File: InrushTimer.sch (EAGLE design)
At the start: 71 parts, among them IC1 TLC272D, IC2 555, IC3 4076N, Q2 TRANSISTOR-FET_2N7002, Q3 TRANSISTOR-FET_2N7002, Q4 TRANSISTOR-FET_2N7002, Q5 TRANSISTOR-FET_2N7002, Q6 DIODES_ZTX451DIODES_ZTX451_0_0, T1 MMBTA05, U1 ROHM_BY_ELEMENT14_BATCH_1_BU4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

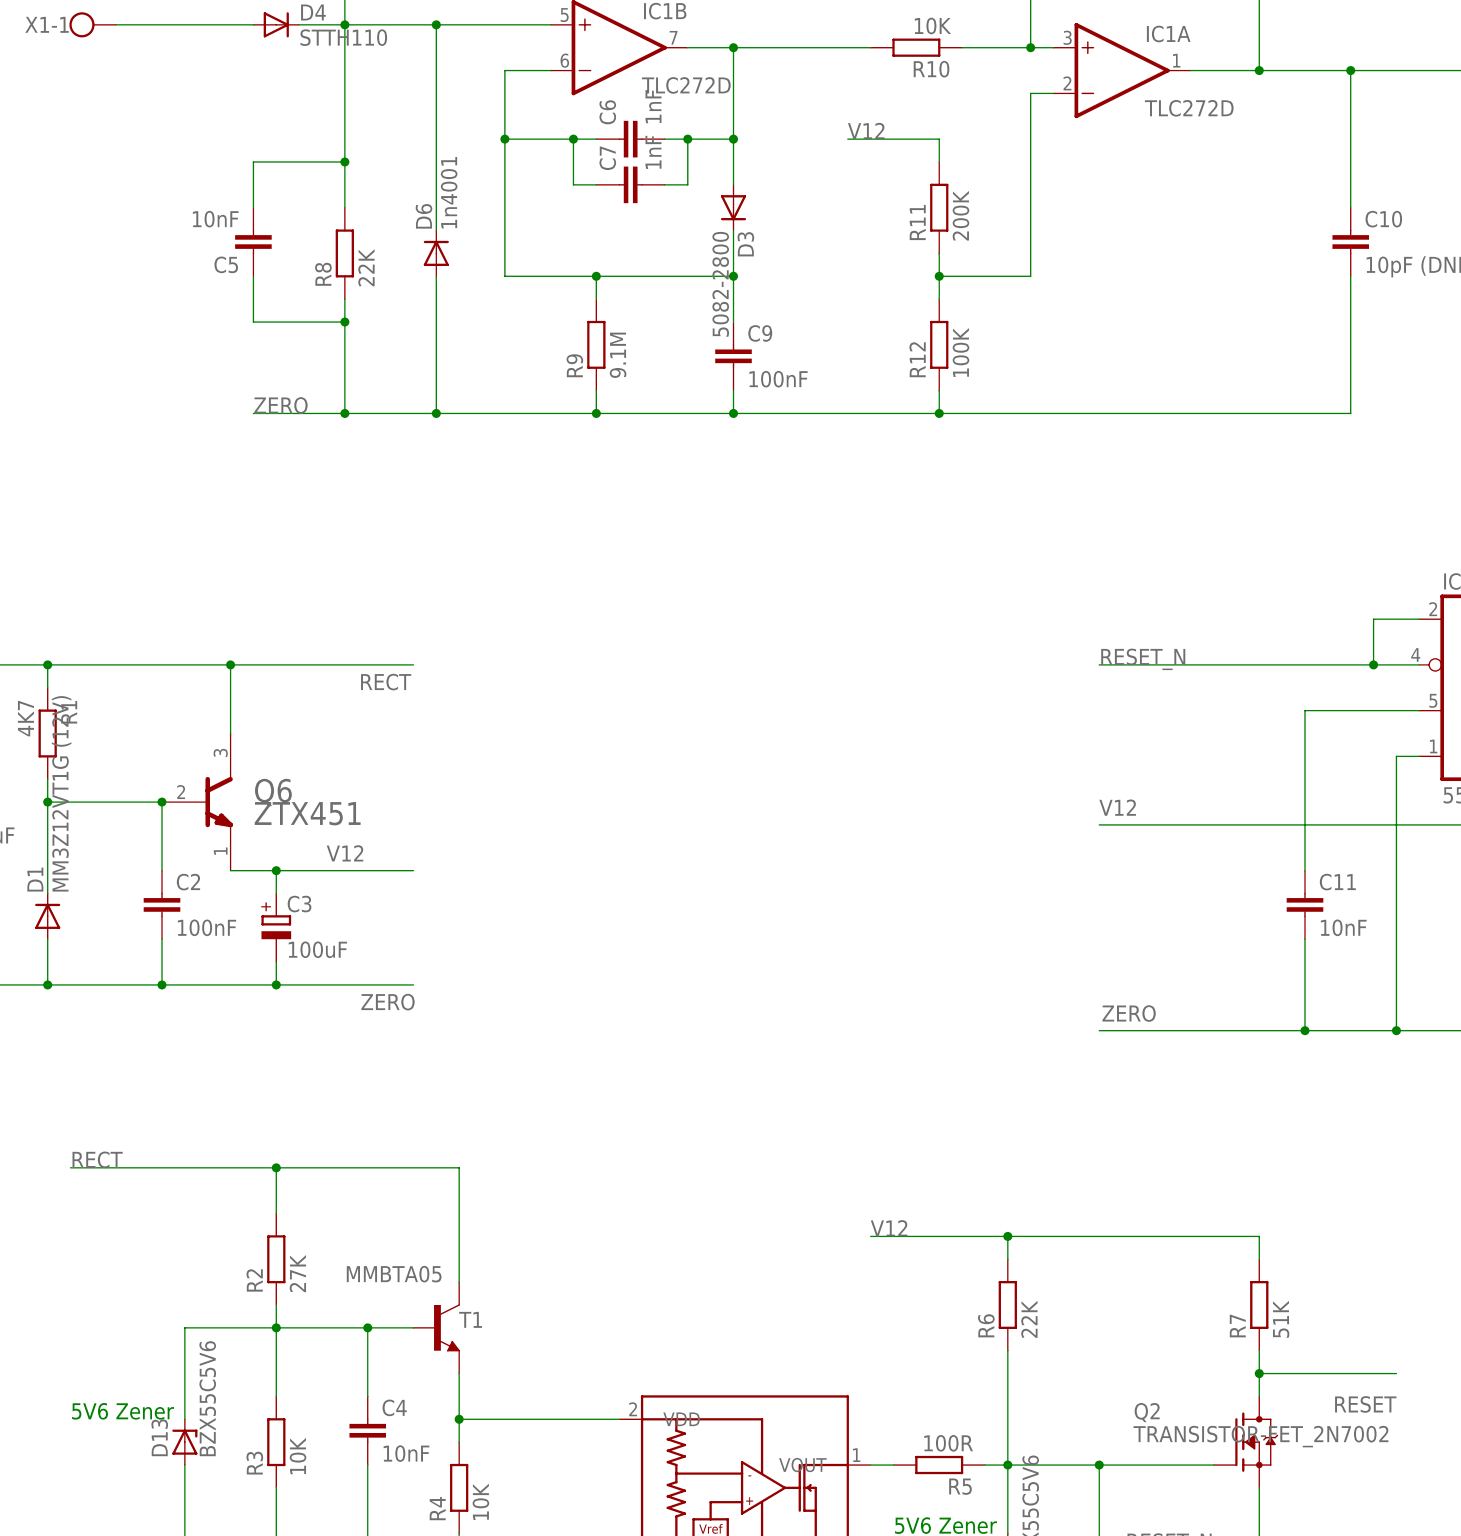
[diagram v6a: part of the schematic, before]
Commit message: Changed pass element to TIP41C and moved some components around to make more space.
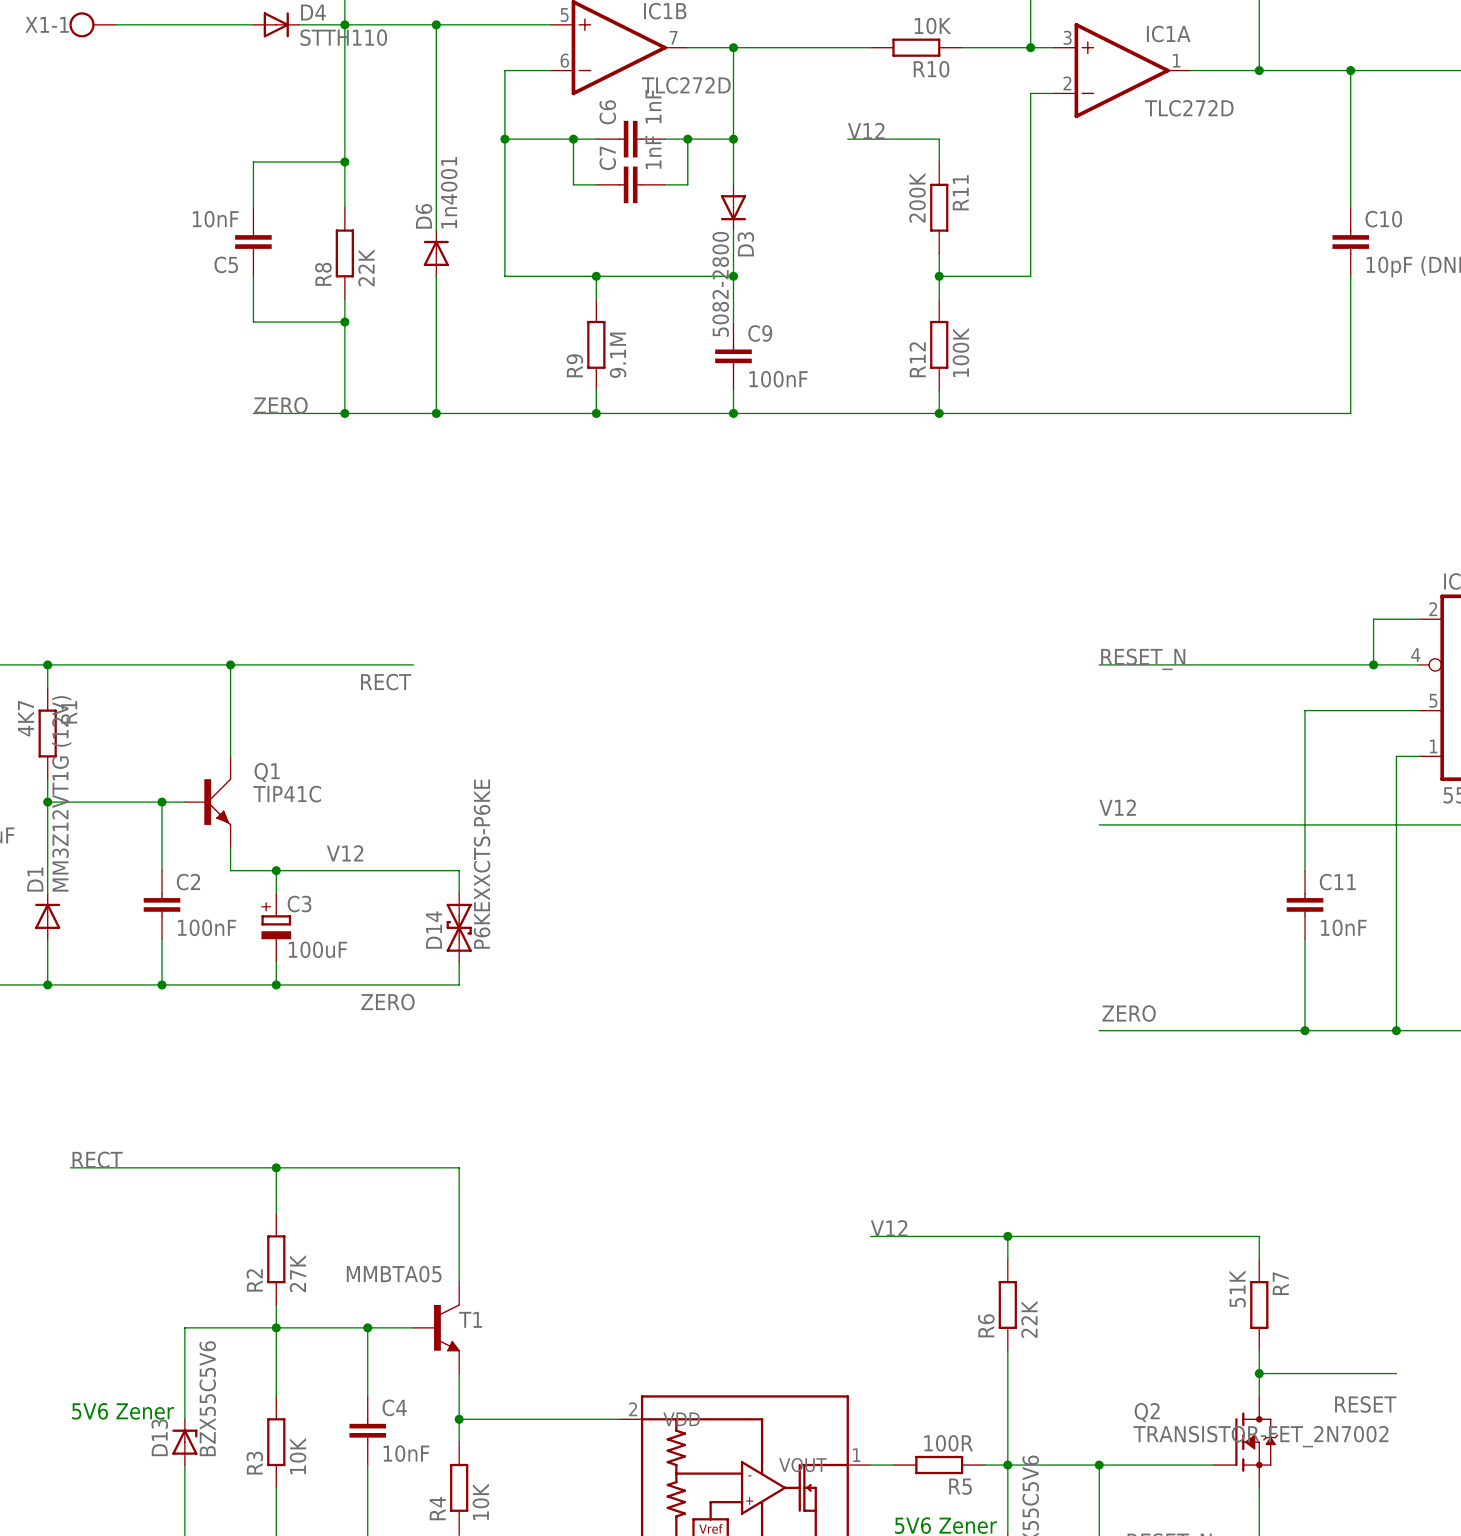
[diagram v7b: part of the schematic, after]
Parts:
- removed Q6: DIODES_ZTX451DIODES_ZTX451_0_0, Diodes - ZTX451:DIODES_ZTX451DIODES_ZTX451_0_0
- added D14: P6KEXXCTS-P6KE, diode:P6KEXXCTS-P6KE
- added Q1: TIP41C, transistor-power:TIP41C
- R7: device rcl:R-EU_0207/2V -> rcl:R-EU_0207/7
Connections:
- net N$8: now also Q1.B; no longer Q6.B
- net RECT: now also Q1.C; no longer Q6.C
- net RESET: now also R7.2; no longer R7.1
- net THRESH: now also R11.2; no longer R11.1
- net V12: now also D14.2, Q1.E, R11.1, R7.1; no longer Q6.E, R11.2, R7.2
- net ZERO: now also D14.1
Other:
- moved on the sheet: R11, R7
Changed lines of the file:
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@@
 <layer number="17" name="Pads" color="2" fill="1" visible="yes" active="no"/>
 <layer number="18" name="Vias" color="2" fill="1" visible="yes" active="no"/>
-<layer number="19" name="Unrouted" color="6" fill="1" visible="yes" active="no"/>
+<layer number="19" name="Unrouted" color="14" fill="1" visible="yes" active="no"/>
 <layer number="20" name="Dimension" color="24" fill="1" visible="yes" active="no"/>
 <layer number="21" name="tPlace" color="15" fill="1" visible="yes" active="no"/>
@@
 <part name="R13" library="rcl" deviceset="R-EU_" device="0207/2V" value="200K"/>
 <part name="R2" library="rcl" deviceset="R-EU_" device="0207/7" value="27K"/>
-<part name="R7" library="rcl" deviceset="R-EU_" device="0207/2V" value="51K"/>
+<part name="R7" library="rcl" deviceset="R-EU_" device="0207/7" value="51K"/>
 <part name="R6" library="rcl" deviceset="R-EU_" device="0207/7" value="22K"/>
 <part name="R3" library="rcl" deviceset="R-EU_" device="0207/2V" value="10K"/>
@@
 <part name="C16" library="rcl" deviceset="C-EU" device="C1206K" value="100nF (DNF)"/>
 <part name="C15" library="rcl" deviceset="C-EU" device="C1206K" value="100nF (DNF)"/>
-<part name="Q6" library="Diodes - ZTX451" deviceset="DIODES_ZTX451" device="DIODES_ZTX451_0_0"/>
 <part name="D13" library="diode" deviceset="ZENER-DIODE" device="DO34-7" value="BZX55C5V6"/>
 <part name="D2" library="diode" deviceset="ZENER-DIODE" device="DO34-7" value="BZX55C5V6"/>
 <part name="D3" library="diode" deviceset="DIODE-" device="DO34-7" value="5082-2800"/>
 <part name="U$1" library="SHoleLib" deviceset="TLP268J" device=""/>
+<part name="D14" library="diode" deviceset="P6KEXXC" device="TS-P6KE" value="P6KEXXCTS-P6KE"/>
+<part name="Q1" library="transistor-power" deviceset="TIP41C" device=""/>
 </parts>
 <sheets>
@@
 <instance part="D5" gate="G$1" x="-66.04" y="93.98" rot="R90"/>
 <instance part="R9" gate="G$1" x="-38.1" y="45.72" rot="R90"/>
-<instance part="R11" gate="G$1" x="0" y="60.96" rot="R90"/>
+<instance part="R11" gate="G$1" x="0" y="60.96" rot="R270"/>
 <instance part="R12" gate="G$1" x="0" y="45.72" rot="R90"/>
 <instance part="IC3" gate="A" x="223.52" y="-7.62"/>
@@
 <instance part="R13" gate="G$1" x="22.86" y="91.44" rot="R180"/>
 <instance part="R2" gate="G$1" x="-73.66" y="-55.88" rot="R90"/>
-<instance part="R7" gate="G$1" x="35.56" y="-60.96" rot="R90"/>
+<instance part="R7" gate="G$1" x="35.56" y="-60.96" rot="R270"/>
 <instance part="R6" gate="G$1" x="7.62" y="-60.96" rot="R90"/>
 <instance part="R3" gate="G$1" x="-73.66" y="-76.2" rot="R90"/>
@@
 <instance part="C16" gate="G$1" x="276.86" y="-15.24"/>
 <instance part="C15" gate="G$1" x="269.24" y="-17.78" rot="R180"/>
-<instance part="Q6" gate="G$0" x="-83.82" y="2.54"/>
 <instance part="D13" gate="G$1" x="-83.82" y="-76.2" rot="R90"/>
 <instance part="D2" gate="G$1" x="7.62" y="-88.9" rot="R90"/>
 <instance part="D3" gate="G$1" x="-22.86" y="60.96" rot="R270"/>
 <instance part="U$1" gate="G$1" x="368.3" y="7.62"/>
+<instance part="D14" gate="1" x="-53.34" y="-20.32" rot="R90"/>
+<instance part="Q1" gate="1" x="-81.28" y="-5.08"/>
 </instances>
 <busses>
@@
 <wire x1="-119.38" y1="10.16" x2="-109.22" y2="10.16" width="0.1524" layer="91"/>
 <junction x="-109.22" y="10.16"/>
-<pinref part="Q6" gate="G$0" pin="C"/>
-<wire x1="-78.74" y1="2.54" x2="-78.74" y2="10.16" width="0.1524" layer="91"/>
+<wire x1="-78.74" y1="0" x2="-78.74" y2="10.16" width="0.1524" layer="91"/>
 <junction x="-78.74" y="10.16"/>
 <pinref part="R1" gate="G$1" pin="1"/>
 <wire x1="-99.06" y1="7.62" x2="-99.06" y2="10.16" width="0.1524" layer="91"/>
 <junction x="-99.06" y="10.16"/>
+<pinref part="Q1" gate="1" pin="C"/>
 </segment>
 <segment>
@@
 <segment>
 <pinref part="D1" gate="G$1" pin="C"/>
-<pinref part="Q6" gate="G$0" pin="B"/>
 <wire x1="-99.06" y1="-5.08" x2="-99.06" y2="-15.24" width="0.1524" layer="91"/>
 <wire x1="-86.36" y1="-5.08" x2="-99.06" y2="-5.08" width="0.1524" layer="91"/>
 <pinref part="C2" gate="G$1" pin="1"/>
 <wire x1="-86.36" y1="-12.7" x2="-86.36" y2="-5.08" width="0.1524" layer="91"/>
-<junction x="-86.36" y="-5.08"/>
 <pinref part="R1" gate="G$1" pin="2"/>
 <wire x1="-99.06" y1="-2.54" x2="-99.06" y2="-5.08" width="0.1524" layer="91"/>
 <junction x="-99.06" y="-5.08"/>
+<pinref part="Q1" gate="1" pin="B"/>
+<wire x1="-83.82" y1="-5.08" x2="-86.36" y2="-5.08" width="0.1524" layer="91"/>
+<junction x="-86.36" y="-5.08"/>
 </segment>
 </net>
@@
 <segment>
 <wire x1="-78.74" y1="-12.7" x2="-73.66" y2="-12.7" width="0.1524" layer="91"/>
-<wire x1="-73.66" y1="-12.7" x2="-58.42" y2="-12.7" width="0.1524" layer="91"/>
+<wire x1="-73.66" y1="-12.7" x2="-53.34" y2="-12.7" width="0.1524" layer="91"/>
 <wire x1="-73.66" y1="-12.7" x2="-73.66" y2="-15.24" width="0.1524" layer="91"/>
 <junction x="-73.66" y="-12.7"/>
 <label x="-68.072" y="-11.684" size="1.778" layer="95"/>
 <pinref part="C3" gate="G$1" pin="+"/>
-<pinref part="Q6" gate="G$0" pin="E"/>
+<pinref part="D14" gate="1" pin="2"/>
+<wire x1="-53.34" y1="-12.7" x2="-53.34" y2="-15.24" width="0.1524" layer="91"/>
+<pinref part="Q1" gate="1" pin="E"/>
+<wire x1="-78.74" y1="-10.16" x2="-78.74" y2="-12.7" width="0.1524" layer="91"/>
 </segment>
 <segment>
@@
 <label x="-7.62" y="-53.34" size="1.778" layer="95"/>
 <wire x1="35.56" y1="-53.34" x2="7.62" y2="-53.34" width="0.1524" layer="91"/>
-<pinref part="R7" gate="G$1" pin="2"/>
 <wire x1="7.62" y1="-53.34" x2="-7.62" y2="-53.34" width="0.1524" layer="91"/>
-<wire x1="35.56" y1="-55.88" x2="35.56" y2="-53.34" width="0.1524" layer="91"/>
 <pinref part="R6" gate="G$1" pin="2"/>
 <wire x1="7.62" y1="-55.88" x2="7.62" y2="-53.34" width="0.1524" layer="91"/>
 <junction x="7.62" y="-53.34"/>
+<pinref part="R7" gate="G$1" pin="1"/>
+<wire x1="35.56" y1="-55.88" x2="35.56" y2="-53.34" width="0.1524" layer="91"/>
 </segment>
 <segment>
@@
 <label x="-10.16" y="68.58" size="1.778" layer="95"/>
 <wire x1="0" y1="68.58" x2="-10.16" y2="68.58" width="0.1524" layer="91"/>
-<pinref part="R11" gate="G$1" pin="2"/>
+<pinref part="R11" gate="G$1" pin="1"/>
 <wire x1="0" y1="66.04" x2="0" y2="68.58" width="0.1524" layer="91"/>
 </segment>
@@
 <junction x="-99.06" y="-25.4"/>
 <wire x1="-86.36" y1="-25.4" x2="-99.06" y2="-25.4" width="0.1524" layer="91"/>
-<wire x1="-73.66" y1="-25.4" x2="-58.42" y2="-25.4" width="0.1524" layer="91"/>
+<wire x1="-73.66" y1="-25.4" x2="-53.34" y2="-25.4" width="0.1524" layer="91"/>
 <junction x="-73.66" y="-25.4"/>
 <label x="-58.166" y="-26.416" size="1.778" layer="95" rot="R180"/>
@@
 <wire x1="-119.38" y1="-25.4" x2="-109.22" y2="-25.4" width="0.1524" layer="91"/>
 <junction x="-109.22" y="-25.4"/>
+<pinref part="D14" gate="1" pin="1"/>
+<wire x1="-53.34" y1="-22.86" x2="-53.34" y2="-25.4" width="0.1524" layer="91"/>
 </segment>
 <segment>
@@
 <wire x1="35.56" y1="-68.58" x2="35.56" y2="-71.12" width="0.1524" layer="91"/>
 <pinref part="Q2" gate="G$1" pin="D"/>
-<pinref part="R7" gate="G$1" pin="1"/>
-<wire x1="35.56" y1="-68.58" x2="35.56" y2="-66.04" width="0.1524" layer="91"/>
+<pinref part="R7" gate="G$1" pin="2"/>
+<wire x1="35.56" y1="-66.04" x2="35.56" y2="-68.58" width="0.1524" layer="91"/>
 <junction x="35.56" y="-68.58"/>
 </segment>
@@
 <wire x1="12.7" y1="73.66" x2="10.16" y2="73.66" width="0.1524" layer="91"/>
 <wire x1="0" y1="53.34" x2="10.16" y2="53.34" width="0.1524" layer="91"/>
-<pinref part="R11" gate="G$1" pin="1"/>
-<wire x1="0" y1="55.88" x2="0" y2="53.34" width="0.1524" layer="91"/>
 <pinref part="R12" gate="G$1" pin="2"/>
 <wire x1="0" y1="50.8" x2="0" y2="53.34" width="0.1524" layer="91"/>
+<pinref part="R11" gate="G$1" pin="2"/>
+<wire x1="0" y1="55.88" x2="0" y2="53.34" width="0.1524" layer="91"/>
 <junction x="0" y="53.34"/>
 </segment>
